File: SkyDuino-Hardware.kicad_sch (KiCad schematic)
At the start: 38 parts, among them J1 24V, J2 BT, J4 Drum, J5 Exhaust, J6 Cooling, J7 Cooling, J8 NTC, Q1 DMN6075S, Q2 DMN6075S, U1 LV3842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

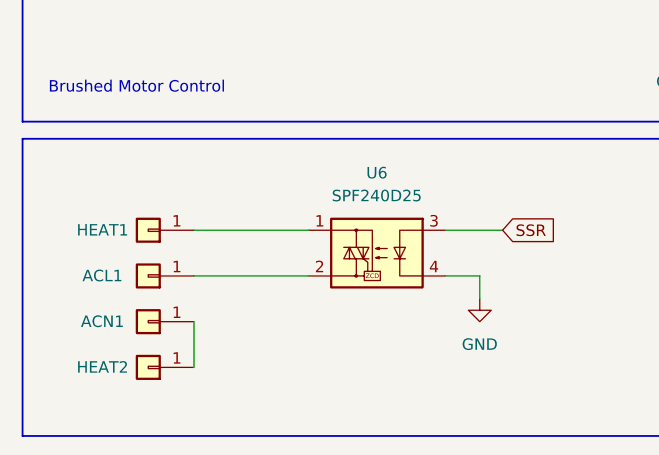
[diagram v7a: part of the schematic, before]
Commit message: Label AC lines
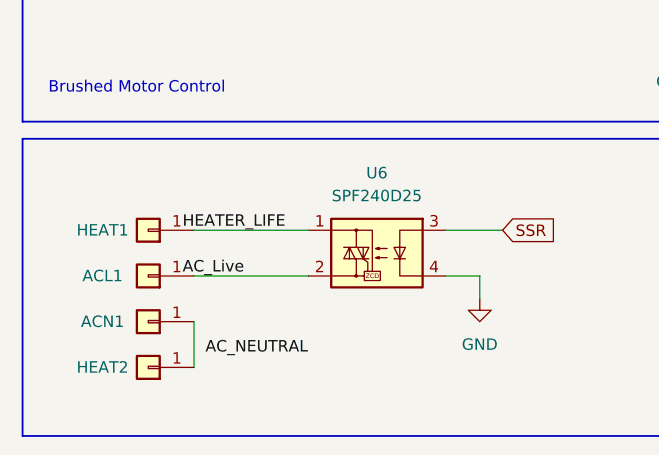
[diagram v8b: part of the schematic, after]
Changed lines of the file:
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@@
+		)
+	)
+	(label "AC_NEUTRAL"
+		(at 34.29 185.42 0)
+		(fields_autoplaced yes)
+		(effects
+			(font
+				(size 1.27 1.27)
+			)
+			(justify left bottom)
+		)
+	)
+	(label "HEATER_LIFE"
+		(at 31.75 171.45 0)
+		(fields_autoplaced yes)
+		(effects
+			(font
+				(size 1.27 1.27)
+			)
+			(justify left bottom)
+		)
+	)
+	(label "AC_Live"
+		(at 31.75 176.53 0)
+		(fields_autoplaced yes)
+		(effects
+			(font
+				(size 1.27 1.27)
+			)
+			(justify left bottom)
 		)
 	)
@@
 			)
 		)
+	)
+	(netclass_flag ""
+		(length 2.54)
+		(shape diamond)
+		(at 44.45 171.45 0)
+		(effects
+			(font
+				(size 1.27 1.27)
+			)
+			(justify left bottom)
+		)
+		(property "Netclass" "AC"
+			(at 44.45 167.386 90)
+			(effects
+				(font
+					(size 1.27 1.27)
+					(italic yes)
+				)
+				(justify left)
+			)
+		)
+	)
+	(netclass_flag ""
+		(length 2.54)
+		(shape diamond)
+		(at 44.45 176.53 180)
+		(effects
+			(font
+				(size 1.27 1.27)
+			)
+			(justify right bottom)
+		)
+		(property "Netclass" "AC"
+			(at 44.45 180.594 90)
+			(effects
+				(font
+					(size 1.27 1.27)
+					(italic yes)
+				)
+				(justify right)
+			)
+		)
+	)
+	(netclass_flag ""
+		(length 2.54)
+		(shape diamond)
+		(at 33.02 181.61 270)
+		(effects
+			(font
+				(size 1.27 1.27)
+			)
+			(justify right bottom)
+		)
+		(property "Netclass" "AC"
+			(at 37.084 181.61 0)
+			(effects
+				(font
+					(size 1.27 1.27)
+					(italic yes)
+				)
+				(justify left)
+			)
+		)
